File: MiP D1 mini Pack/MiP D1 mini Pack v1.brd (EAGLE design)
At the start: 41.4 x 63.8 mm, 6 parts, among them J2 D1 mini, J3 Debug

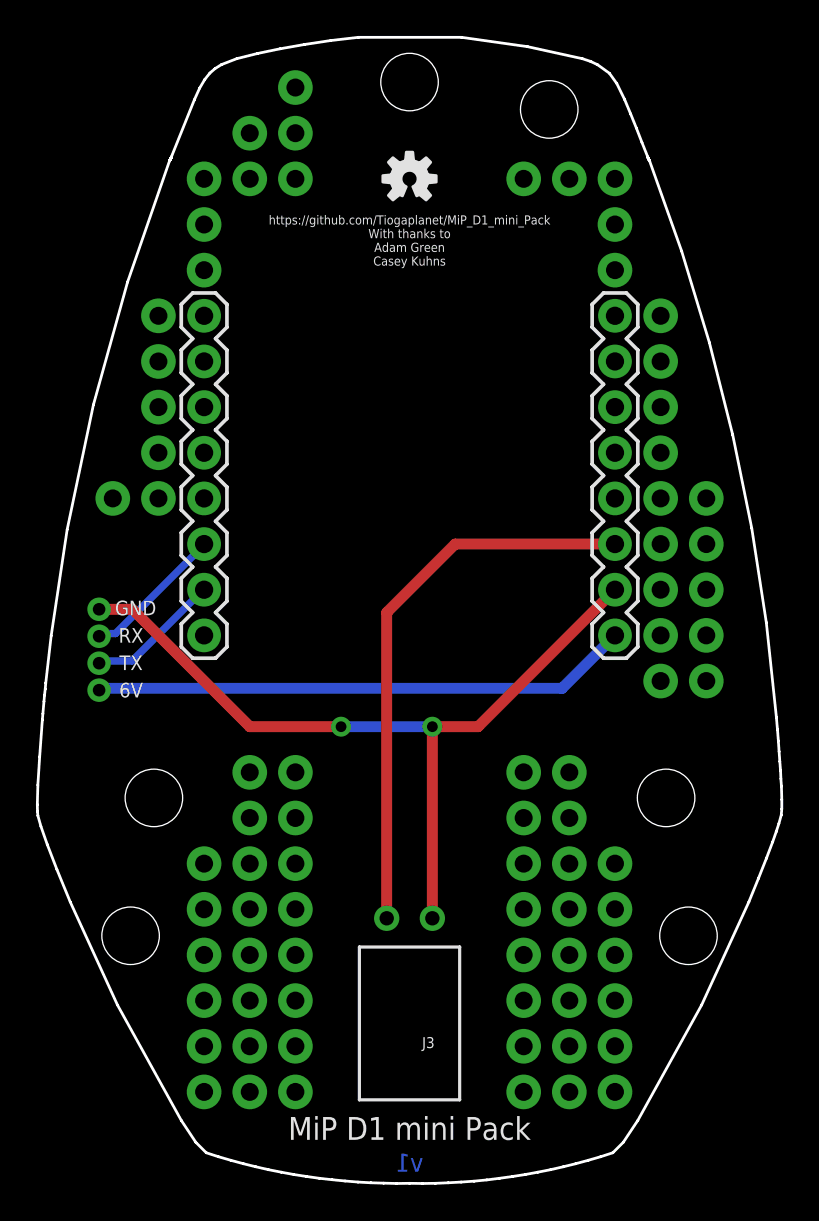
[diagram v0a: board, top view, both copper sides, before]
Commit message: Moved the debug connector
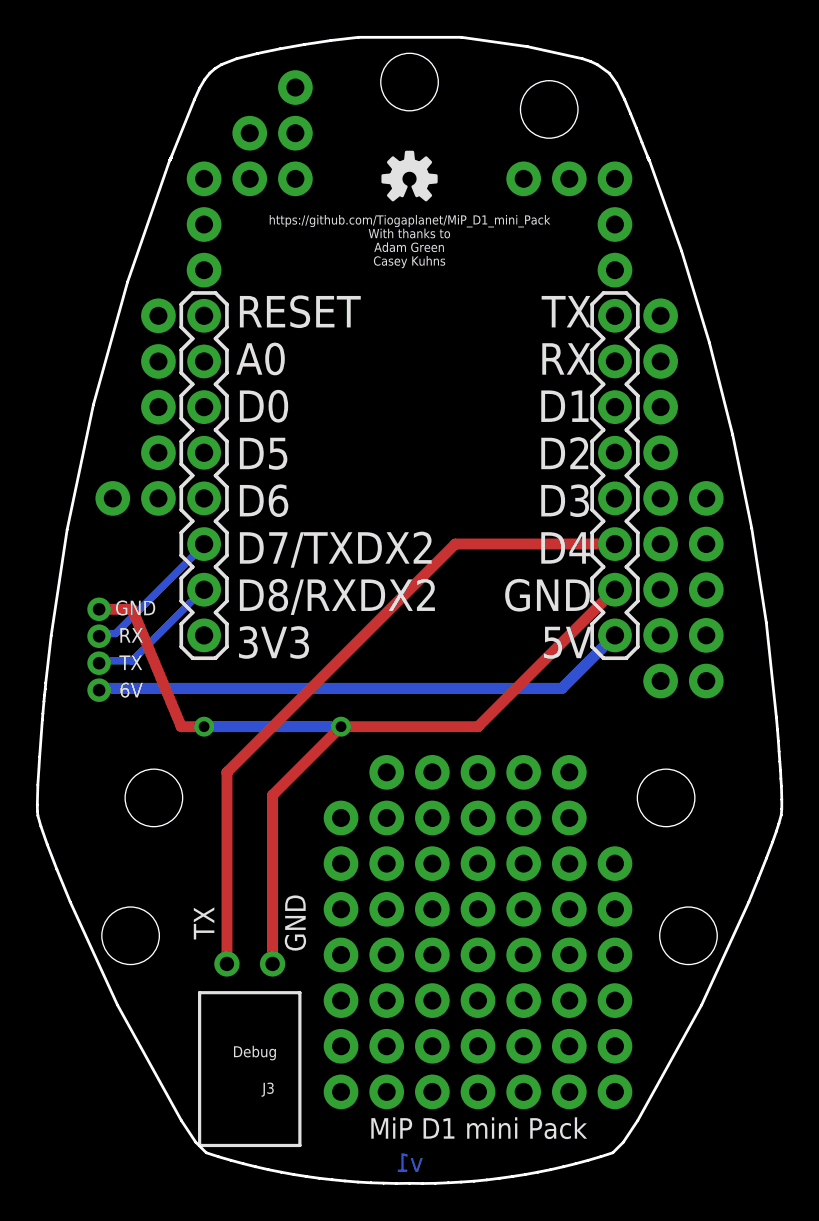
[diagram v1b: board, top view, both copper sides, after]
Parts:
- moved J3 9.25 mm to (15.2, 7.62)
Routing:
- net N$4: track 31.3 -> 37.5 mm
- net GND: track 45.2 -> 51.0 mm
